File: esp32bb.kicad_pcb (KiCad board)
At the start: 2 copper layers, 43.2 x 61 mm, 33 parts, among them CON1 Micro_SD_Card, IC1 FT232RQ, J1 CONN_01X18, P1 CONN_01X17, P3 USB_OTG, Q1 MMBT3904, Q2 MMBT3904, SW1 SWITCH_SPST, SW2 SWITCH_SPST, U1 ESP32-WROOM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

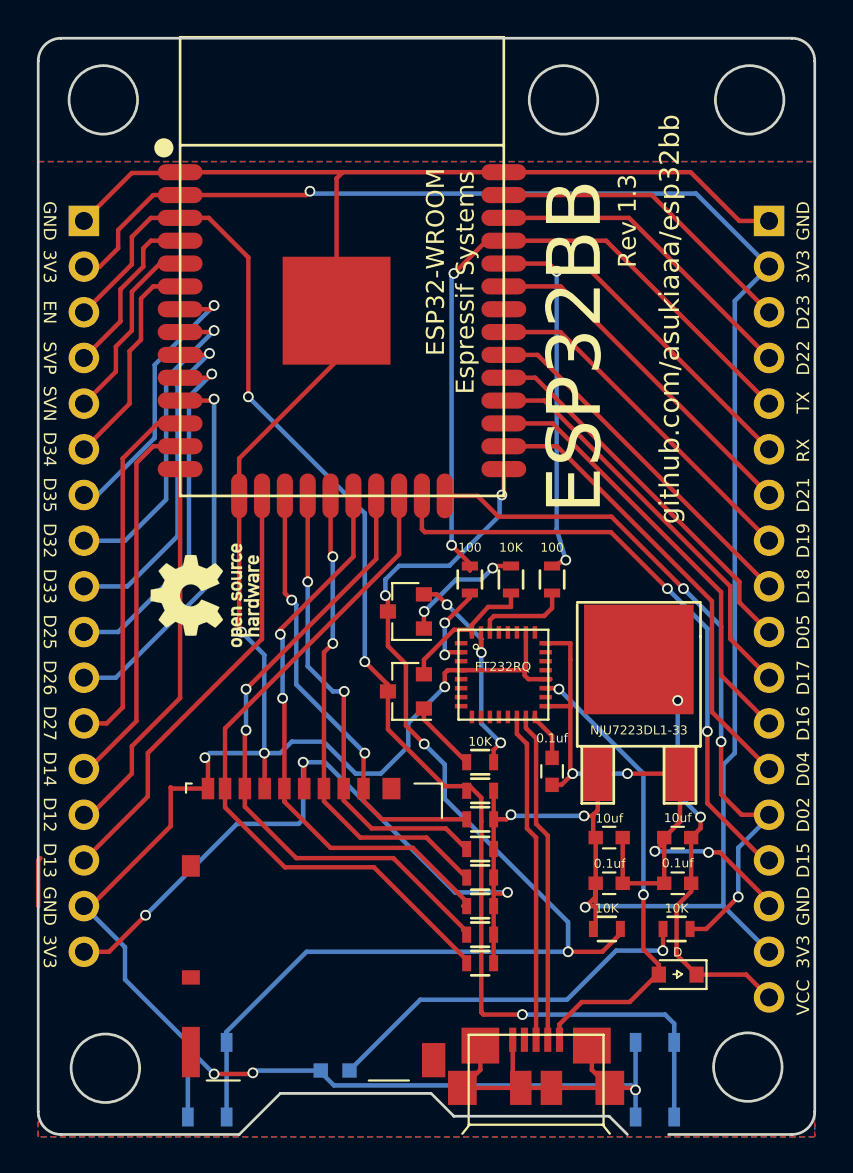
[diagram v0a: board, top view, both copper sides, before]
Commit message: Change holls size and position and add dimension
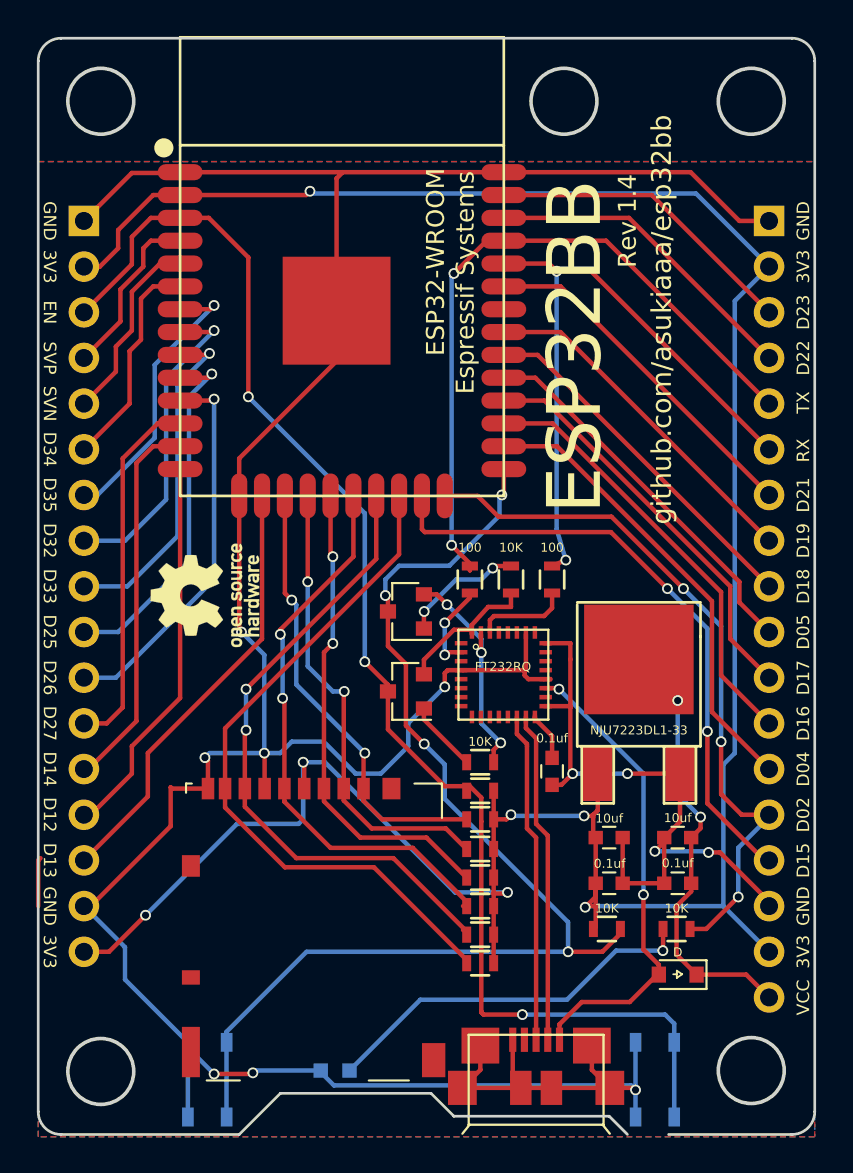
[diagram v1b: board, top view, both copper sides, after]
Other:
- outline, holes or cut-outs redrawn
- board text added: "Rev 1.4"
- board text removed: "Rev 1.3"
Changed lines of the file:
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@@
     (links 115)
     (no_connects 0)
-    (area 147.366667 58.461 195.533334 126.269142)
+    (area 138.257687 47.6936 217.291515 126.269142)
     (thickness 1.6)
-    (drawings 96)
+    (drawings 104)
     (tracks 575)
     (zones 0)
@@
   )
   (layers
-    (0 F.Cu signal)
-    (31 B.Cu signal)
+    (0 F.Cu signal hide)
+    (31 B.Cu signal hide)
     (32 B.Adhes user)
     (33 F.Adhes user)
@@
     (trace_min 0.2)
     (segment_width 0.2)
-    (edge_width 0.15)
+    (edge_width 0.2)
     (via_size 0.6)
     (via_drill 0.4)
@@
     (descr http://akizukidenshi.com/download/ds/alps/SKRPACE010.pdf)
     (tags "Tactile Switch")
-    (fp_text reference SW1 (at 0.06 2.85 90) (layer B.Fab)
+    (fp_text reference SW1 (at 0.06 2.85 90) (layer B.Fab) hide
       (effects (font (size 1.5 1.5) (thickness 0.15)) (justify mirror))
     )
@@
       (effects (font (size 1 1) (thickness 0.15)) (justify mirror))
     )
-    (fp_text value CONN_01X17 (at 0 -43.03 180) (layer B.Fab)
+    (fp_text value CONN_01X17 (at 0 -43.03 180) (layer B.Fab) hide
       (effects (font (size 1 1) (thickness 0.15)) (justify mirror))
     )
@@
     (descr http://akizukidenshi.com/download/ds/alps/SKRPACE010.pdf)
     (tags "Tactile Switch")
-    (fp_text reference SW2 (at 0.06 2.85 90) (layer B.Fab)
+    (fp_text reference SW2 (at 0.06 2.85 90) (layer B.Fab) hide
       (effects (font (size 1.5 1.5) (thickness 0.15)) (justify mirror))
     )
@@
     )
   )
+  (dimension 3.6576 (width 0.3) (layer F.Fab)
+    (gr_text "3.658 mm" (at 144.0434 63.9572 90) (layer F.Fab)
+      (effects (font (size 1.5 1.5) (thickness 0.3)))
+    )
+    (feature1 (pts (xy 153.3398 62.6364) (xy 145.001 62.6364)))
+    (feature2 (pts (xy 153.3398 66.294) (xy 145.001 66.294)))
+    (crossbar (pts (xy 147.701 66.294) (xy 147.701 62.6364)))
+    (arrow1a (pts (xy 147.701 62.6364) (xy 148.287421 63.762904)))
+    (arrow1b (pts (xy 147.701 62.6364) (xy 147.114579 63.762904)))
+    (arrow2a (pts (xy 147.701 66.294) (xy 148.287421 65.167496)))
+    (arrow2b (pts (xy 147.701 66.294) (xy 147.114579 65.167496)))
+  )
+  (gr_circle (center 153.3398 64.4652) (end 154.6606 65.7352) (layer Edge.Cuts) (width 0.2))
+  (gr_circle (center 189.5094 118.364) (end 190.8302 119.634) (layer Edge.Cuts) (width 0.2))
+  (gr_circle (center 153.3398 118.4148) (end 154.6606 119.6848) (layer Edge.Cuts) (width 0.2))
+  (gr_circle (center 189.5094 64.4652) (end 190.8302 65.7352) (layer Edge.Cuts) (width 0.2))
+  (gr_circle (center 179.0954 64.4652) (end 180.4162 65.7352) (layer Edge.Cuts) (width 0.2))
+  (dimension 54.0004 (width 0.3) (layer F.Fab)
+    (gr_text "54.000 mm" (at 199.089 91.4146 90) (layer F.Fab)
+      (effects (font (size 1.5 1.5) (thickness 0.3)))
+    )
+    (feature1 (pts (xy 189.5602 64.4144) (xy 200.439 64.4144)))
+    (feature2 (pts (xy 189.5602 118.4148) (xy 200.439 118.4148)))
+    (crossbar (pts (xy 197.739 118.4148) (xy 197.739 64.4144)))
+    (arrow1a (pts (xy 197.739 64.4144) (xy 198.325421 65.540904)))
+    (arrow1b (pts (xy 197.739 64.4144) (xy 197.152579 65.540904)))
+    (arrow2a (pts (xy 197.739 118.4148) (xy 198.325421 117.288296)))
+    (arrow2b (pts (xy 197.739 118.4148) (xy 197.152579 117.288296)))
+  )
+  (dimension 3.4544 (width 0.3) (layer F.Fab)
+    (gr_text "3.454 mm" (at 211.5058 62.6364 90) (layer F.Fab)
+      (effects (font (size 1.5 1.5) (thickness 0.3)))
+    )
+    (feature1 (pts (xy 198.1962 60.96) (xy 210.091 60.96)))
+    (feature2 (pts (xy 198.1962 64.4144) (xy 210.091 64.4144)))
+    (crossbar (pts (xy 207.391 64.4144) (xy 207.391 60.96)))
+    (arrow1a (pts (xy 207.391 60.96) (xy 207.977421 62.086504)))
+    (arrow1b (pts (xy 207.391 60.96) (xy 206.804579 62.086504)))
+    (arrow2a (pts (xy 207.391 64.4144) (xy 207.977421 63.287896)))
+    (arrow2b (pts (xy 207.391 64.4144) (xy 206.804579 63.287896)))
+  )
+  (dimension 3.4544 (width 0.3) (layer F.Fab)
+    (gr_text "3.454 mm" (at 199.4662 55.8292) (layer F.Fab)
+      (effects (font (size 1.5 1.5) (thickness 0.3)))
+    )
+    (feature1 (pts (xy 193.0146 54.2036) (xy 193.0146 58.58)))
+    (feature2 (pts (xy 189.5602 54.2036) (xy 189.5602 58.58)))
+    (crossbar (pts (xy 189.5602 55.88) (xy 193.0146 55.88)))
+    (arrow1a (pts (xy 193.0146 55.88) (xy 191.888096 56.466421)))
+    (arrow1b (pts (xy 193.0146 55.88) (xy 191.888096 55.293579)))
+    (arrow2a (pts (xy 189.5602 55.88) (xy 190.686704 56.466421)))
+    (arrow2b (pts (xy 189.5602 55.88) (xy 190.686704 55.293579)))
+  )
+  (dimension 10.4648 (width 0.3) (layer F.Fab)
+    (gr_text "10.465 mm" (at 172.1866 57.0992) (layer F.Fab)
+      (effects (font (size 1.5 1.5) (thickness 0.3)))
+    )
+    (feature1 (pts (xy 179.0954 64.3636) (xy 179.0954 55.1104)))
+    (feature2 (pts (xy 189.5602 64.3636) (xy 189.5602 55.1104)))
+    (crossbar (pts (xy 189.5602 57.8104) (xy 179.0954 57.8104)))
+    (arrow1a (pts (xy 179.0954 57.8104) (xy 180.221904 57.223979)))
+    (arrow1b (pts (xy 179.0954 57.8104) (xy 180.221904 58.396821)))
+    (arrow2a (pts (xy 189.5602 57.8104) (xy 188.433696 57.223979)))
+    (arrow2b (pts (xy 189.5602 57.8104) (xy 188.433696 58.396821)))
+  )
+  (dimension 36.2204 (width 0.3) (layer F.Fab)
+    (gr_text "36.220 mm" (at 171.45 52.8536) (layer F.Fab)
+      (effects (font (size 1.5 1.5) (thickness 0.3)))
+    )
+    (feature1 (pts (xy 153.3398 64.3636) (xy 153.3398 51.5036)))
+    (feature2 (pts (xy 189.5602 64.3636) (xy 189.5602 51.5036)))
+    (crossbar (pts (xy 189.5602 54.2036) (xy 153.3398 54.2036)))
+    (arrow1a (pts (xy 153.3398 54.2036) (xy 154.466304 53.617179)))
+    (arrow1b (pts (xy 153.3398 54.2036) (xy 154.466304 54.790021)))
+    (arrow2a (pts (xy 189.5602 54.2036) (xy 188.433696 53.617179)))
+    (arrow2b (pts (xy 189.5602 54.2036) (xy 188.433696 54.790021)))
+  )
+  (dimension 60.96 (width 0.3) (layer F.Fab)
+    (gr_text "60.960 mm" (at 205.0834 91.44 90) (layer F.Fab)
+      (effects (font (size 1.5 1.5) (thickness 0.3)))
+    )
+    (feature1 (pts (xy 193.0654 60.96) (xy 206.4334 60.96)))
+    (feature2 (pts (xy 193.0654 121.92) (xy 206.4334 121.92)))
+    (crossbar (pts (xy 203.7334 121.92) (xy 203.7334 60.96)))
+    (arrow1a (pts (xy 203.7334 60.96) (xy 204.319821 62.086504)))
+    (arrow1b (pts (xy 203.7334 60.96) (xy 203.146979 62.086504)))
+    (arrow2a (pts (xy 203.7334 121.92) (xy 204.319821 120.793496)))
+    (arrow2b (pts (xy 203.7334 121.92) (xy 203.146979 120.793496)))
+  )
+  (dimension 43.18 (width 0.3) (layer F.Fab)
+    (gr_text "43.180 mm" (at 171.4246 49.0436) (layer F.Fab)
+      (effects (font (size 1.5 1.5) (thickness 0.3)))
+    )
+    (feature1 (pts (xy 193.0146 60.96) (xy 193.0146 47.6936)))
+    (feature2 (pts (xy 149.8346 60.96) (xy 149.8346 47.6936)))
+    (crossbar (pts (xy 149.8346 50.3936) (xy 193.0146 50.3936)))
+    (arrow1a (pts (xy 193.0146 50.3936) (xy 191.888096 50.980021)))
+    (arrow1b (pts (xy 193.0146 50.3936) (xy 191.888096 49.807179)))
+    (arrow2a (pts (xy 149.8346 50.3936) (xy 150.961104 50.980021)))
+    (arrow2b (pts (xy 149.8346 50.3936) (xy 150.961104 49.807179)))
+  )
   (gr_text RX (at 192.405 83.8835 90) (layer F.SilkS)
     (effects (font (size 0.7 0.7) (thickness 0.175)))
@@
     (effects (font (size 0.7 0.7) (thickness 0.175)))
   )
-  (gr_circle (center 153.4795 64.389) (end 155.3845 64.389) (layer Edge.Cuts) (width 0.15))
-  (gr_circle (center 189.4205 64.389) (end 191.3255 64.389) (layer Edge.Cuts) (width 0.15))
   (gr_text ESP32BB (at 179.705 78.105 90) (layer F.SilkS)
     (effects (font (size 3 3) (thickness 0.5)))
@@
   (gr_line (start 191.77 121.92) (end 184.912 121.92) (angle 90) (layer Edge.Cuts) (width 0.15))
   (gr_line (start 151.13 60.96) (end 191.77 60.96) (angle 90) (layer Edge.Cuts) (width 0.15))
-  (gr_circle (center 179.07 64.389) (end 180.975 64.389) (layer Edge.Cuts) (width 0.15))
   (gr_text GND (at 192.3542 71.12 90) (layer B.SilkS)
     (effects (font (size 0.7 0.7) (thickness 0.175)) (justify mirror))
   )
-  (gr_text "Rev 1.3" (at 182.626 71.12 90) (layer F.SilkS)
+  (gr_text "Rev 1.4" (at 182.626 71.12 90) (layer F.SilkS)
     (effects (font (size 1 1) (thickness 0.2)))
   )
-  (gr_text "Rev 1.3" (at 177.8 119.761) (layer B.SilkS)
+  (gr_text "Rev 1.4" (at 177.8 119.761) (layer B.SilkS)
     (effects (font (size 1 1) (thickness 0.2)) (justify mirror))
   )
@@
     (effects (font (size 1.8 1.8) (thickness 0.4)) (justify mirror))
   )
-  (gr_text github.com/asukiaaa/esp32bb (at 184.9755 76.581 90) (layer F.SilkS)
+  (gr_text github.com/asukiaaa/esp32bb (at 184.531 76.6064 90) (layer F.SilkS)
     (effects (font (size 1.1 1.1) (thickness 0.2)))
   )
@@
     (effects (font (size 0.7 0.7) (thickness 0.175)) (justify mirror))
   )
-  (gr_circle (center 189.3189 118.1735) (end 191.2239 118.1735) (layer Edge.Cuts) (width 0.15))
-  (gr_circle (center 153.5938 118.237) (end 155.4988 118.237) (layer Edge.Cuts) (width 0.15))
   (gr_arc (start 191.77 120.65) (end 193.04 120.65) (angle 90) (layer Edge.Cuts) (width 0.15))
   (gr_arc (start 151.13 120.65) (end 151.13 121.92) (angle 90) (layer Edge.Cuts) (width 0.15))
